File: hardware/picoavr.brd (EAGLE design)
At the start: 36.4 x 18.3 mm, 25 parts, among them IC1 MCP1703CB, Q2 12mhz, SW1 SPST_TACT-KMR2, U3 ATMEGA328P, X1 Micro USB

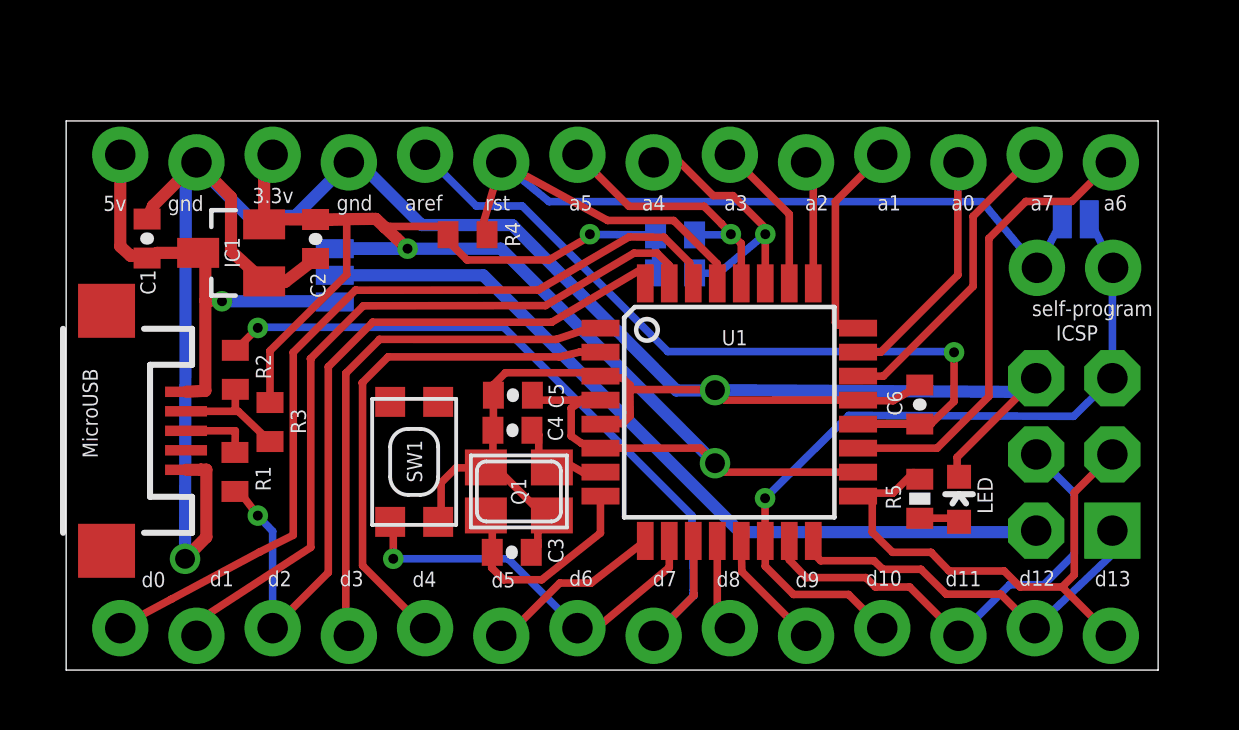
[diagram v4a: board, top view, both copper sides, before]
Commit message: fix pin spacing
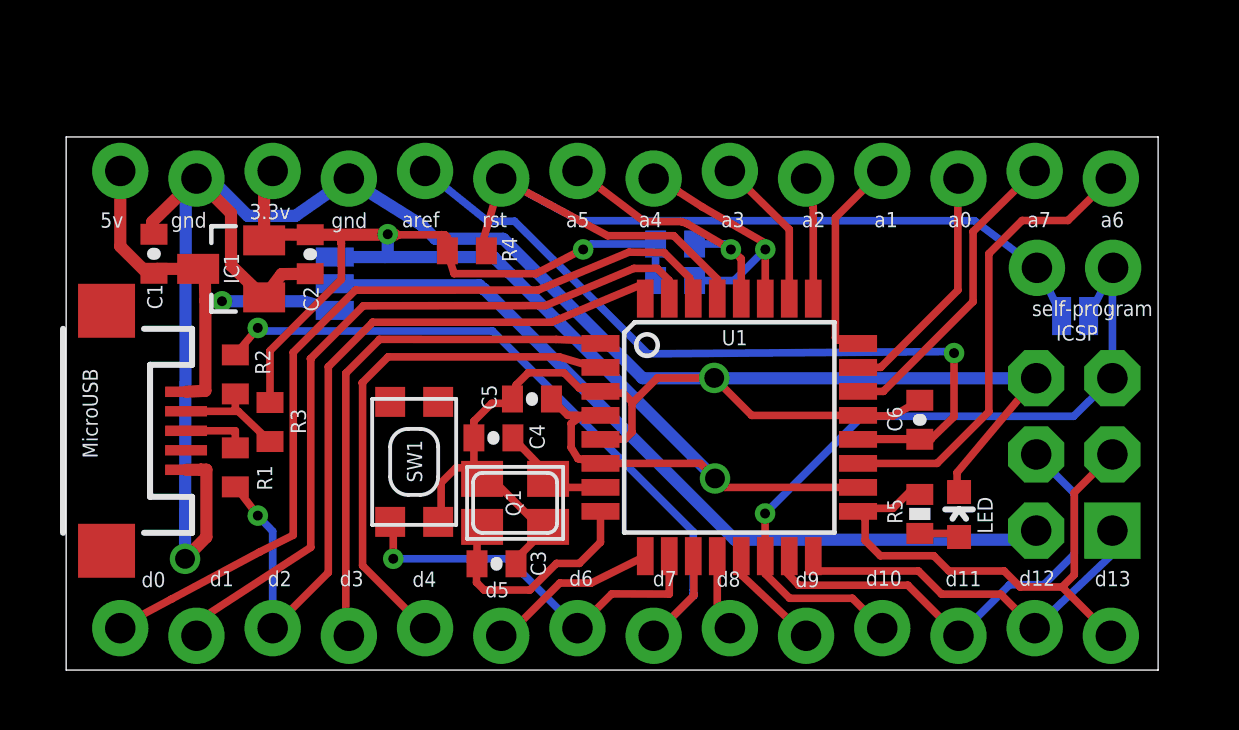
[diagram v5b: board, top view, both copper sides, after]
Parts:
- moved SJ2 3.23 mm to (33.7, 11.8)
- moved C3 0.68 mm to (14.3, 7.74)
- moved C5 0.65 mm to (15.6, 9.04)
- moved C4 0.64 mm to (14.4, 3.54)
- moved C1 0.56 mm to (2.96, 13.9)
- moved JP3 0.54 mm to (1.84, 16.5)
- moved C2 0.54 mm to (8.17, 13.9)
- moved R4 0.53 mm to (13.4, 14.0)
- moved IC1 0.53 mm to (5.54, 13.4)
- moved C6 0.51 mm to (28.5, 8.34)
- moved LED 0.51 mm to (29.8, 5.18)
- moved R5 0.51 mm to (28.5, 5.20)
- moved U3 0.51 mm to (22.1, 8.09)
- moved Q2 0.40 mm to (15.0, 5.57)
- moved R7 0.30 mm to (20.3, 14.2)
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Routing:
- net VCC: track 59.8 -> 56.4 mm
- net ISP_RESET: track 26.9 -> 25.6 mm
- net USB_VBUS: track 15.9 -> 14.8 mm
- net A0: track 8.16 -> 9.16 mm
- net RESET: track 33.1 -> 32.1 mm
- net N$5: track 7.43 -> 8.28 mm
- net SDA: track 8.72 -> 9.48 mm
- net GND: track 93.0 -> 93.7 mm
- net N$6: track 3.54 -> 4.25 mm
- net USB_DMINUS: track 26.8 -> 26.2 mm
- net B0: track 3.08 -> 2.57 mm
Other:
- board size 36.4 x 18.3 mm -> 36.4 x 17.8 mm

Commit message: tweaked dimensions
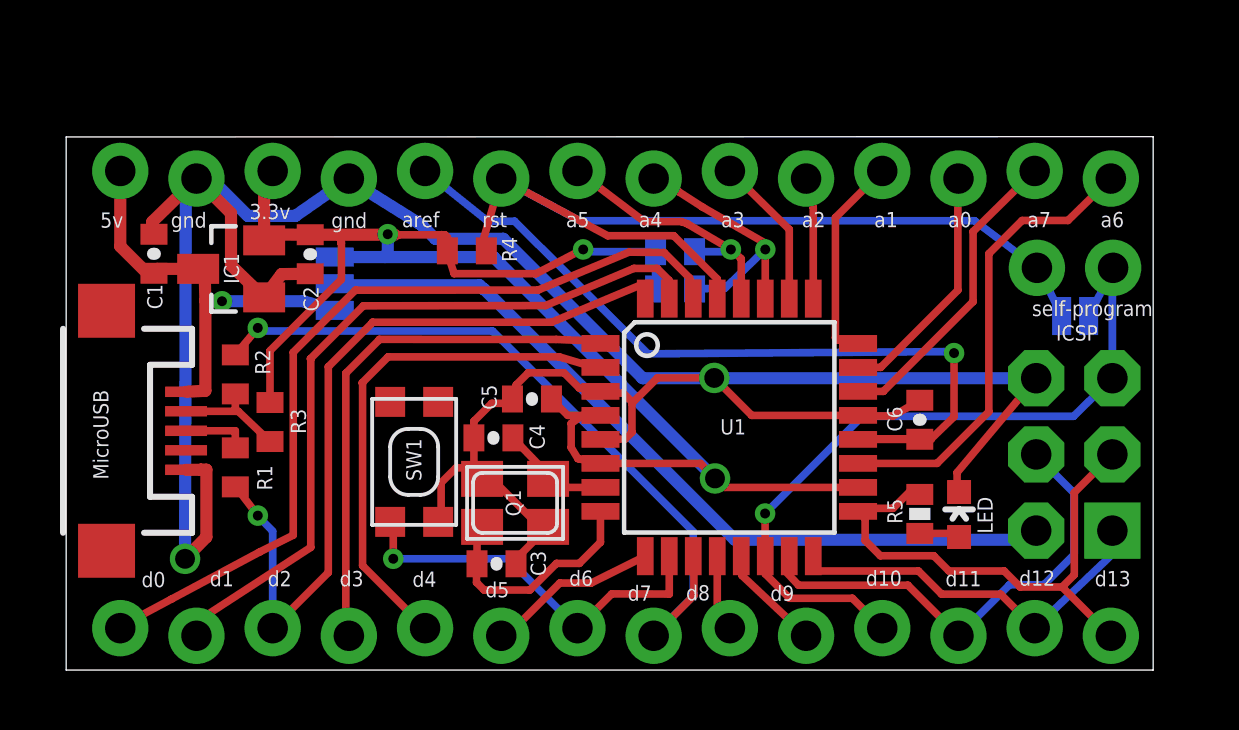
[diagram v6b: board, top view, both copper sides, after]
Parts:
- JSP: value (none) -> ICSP
- moved R6 0.28 mm to (20.3, 12.7)
- moved R7 0.25 mm to (20.3, 13.9)
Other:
- board size 36.4 x 17.8 mm -> 36.2 x 17.8 mm
